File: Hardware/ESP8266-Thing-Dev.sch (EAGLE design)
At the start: 69 parts, among them J1 DNP, Q1 MMBT2222A, Q2 MMBT2222A, U1 AP2112K-3.3V, U2 ESP8266, U3 AT25SF041-SOIC8, U4 FTS31XS-U, Y1 26MHz

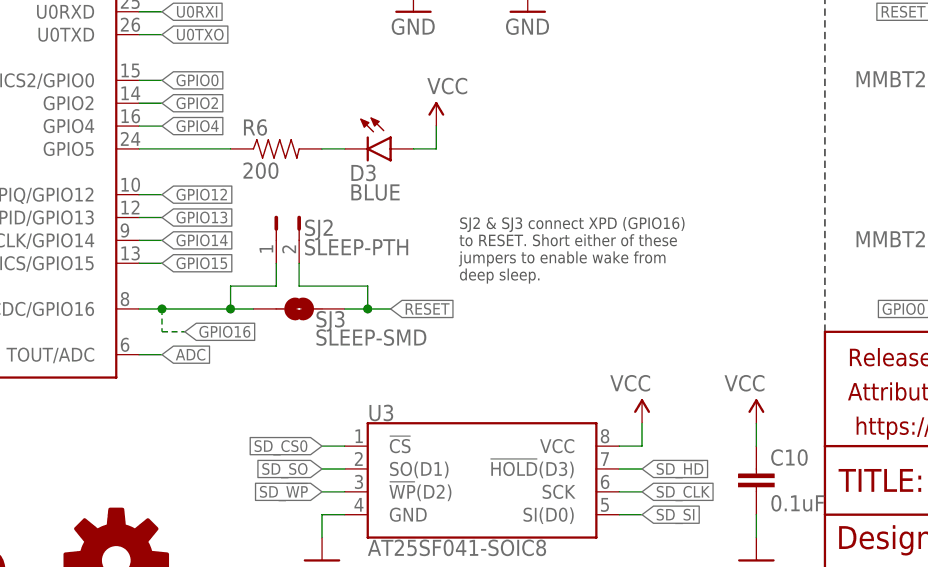
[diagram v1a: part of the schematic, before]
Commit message: Removing SJ3 - SMD sleep jumper
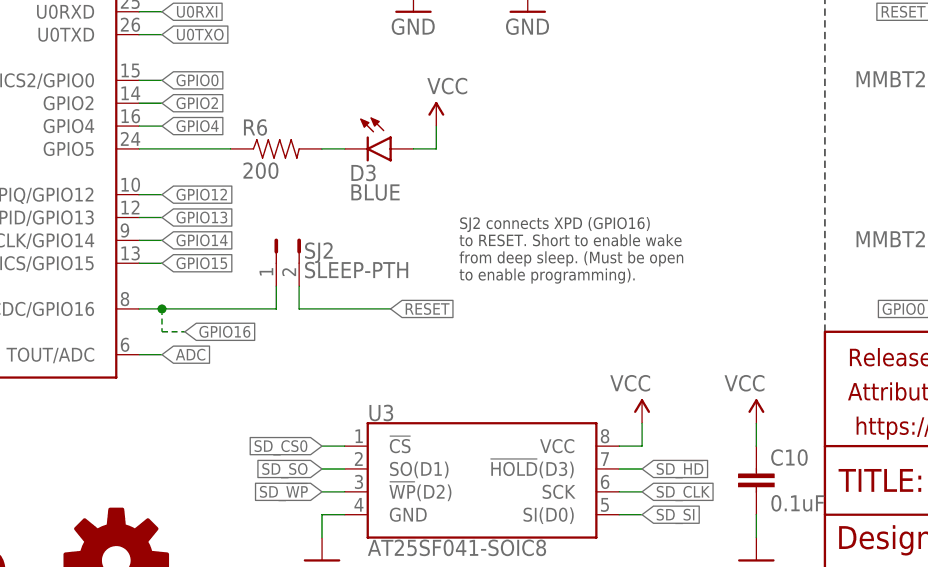
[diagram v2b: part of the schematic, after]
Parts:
- removed SJ3: SLEEP-SMD, SparkFun-Passives:JUMPER-PAD-2-NO
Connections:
- net GPIO16: no longer SJ3.1
- net RESET: no longer SJ3.2
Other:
- note added: "SJ2 connects XPD (GPIO16) to RESET. Short to enable wake from deep sleep. (Must be open to enable programming)."
- note removed: "SJ2 & SJ3 connect XPD (GPIO16) to RESET. Short either of these jumpers to enable wake from deep sleep."
- moved on the sheet: SJ2

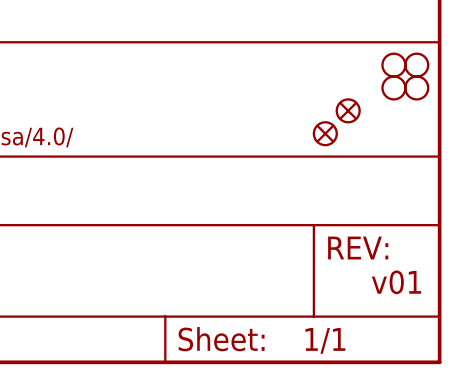
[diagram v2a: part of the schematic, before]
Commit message: Adjusting label header silk a bit
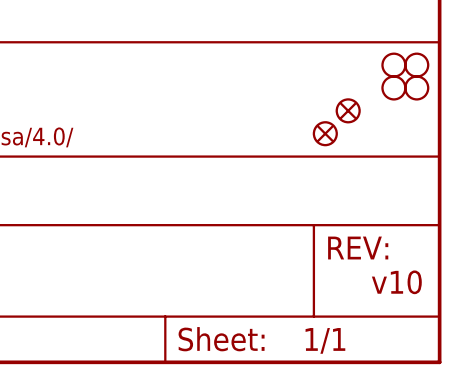
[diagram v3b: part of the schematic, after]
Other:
- note added: "v10"
- note removed: "v01"
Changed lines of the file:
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@@
 <grid distance="0.1" unitdist="inch" unit="inch" style="lines" multiple="1" display="no" altdistance="0.01" altunitdist="inch" altunit="inch"/>
 <layers>
-<layer number="1" name="Top" color="4" fill="1" visible="yes" active="no"/>
-<layer number="2" name="Route2" color="1" fill="3" visible="yes" active="no"/>
-<layer number="3" name="Route3" color="4" fill="3" visible="yes" active="no"/>
-<layer number="4" name="Route4" color="1" fill="4" visible="yes" active="no"/>
-<layer number="5" name="Route5" color="4" fill="4" visible="yes" active="no"/>
-<layer number="6" name="Route6" color="1" fill="8" visible="yes" active="no"/>
-<layer number="7" name="Route7" color="4" fill="8" visible="yes" active="no"/>
-<layer number="8" name="Route8" color="1" fill="2" visible="yes" active="no"/>
-<layer number="9" name="Route9" color="4" fill="2" visible="yes" active="no"/>
-<layer number="10" name="Route10" color="1" fill="7" visible="yes" active="no"/>
-<layer number="11" name="Route11" color="4" fill="7" visible="yes" active="no"/>
-<layer number="12" name="Route12" color="1" fill="5" visible="yes" active="no"/>
-<layer number="13" name="Route13" color="4" fill="5" visible="yes" active="no"/>
-<layer number="14" name="Route14" color="1" fill="6" visible="yes" active="no"/>
-<layer number="15" name="Route15" color="4" fill="6" visible="yes" active="no"/>
-<layer number="16" name="Bottom" color="1" fill="1" visible="yes" active="no"/>
-<layer number="17" name="Pads" color="2" fill="1" visible="yes" active="no"/>
-<layer number="18" name="Vias" color="2" fill="1" visible="yes" active="no"/>
-<layer number="19" name="Unrouted" color="6" fill="1" visible="yes" active="no"/>
-<layer number="20" name="Dimension" color="15" fill="1" visible="yes" active="no"/>
-<layer number="21" name="tPlace" color="16" fill="1" visible="yes" active="no"/>
-<layer number="22" name="bPlace" color="14" fill="1" visible="yes" active="no"/>
-<layer number="23" name="tOrigins" color="15" fill="1" visible="yes" active="no"/>
-<layer number="24" name="bOrigins" color="15" fill="1" visible="yes" active="no"/>
-<layer number="25" name="tNames" color="7" fill="1" visible="yes" active="no"/>
-<layer number="26" name="bNames" color="7" fill="1" visible="yes" active="no"/>
-<layer number="27" name="tValues" color="7" fill="1" visible="yes" active="no"/>
-<layer number="28" name="bValues" color="7" fill="1" visible="yes" active="no"/>
+<layer number="1" name="Top" color="4" fill="1" visible="no" active="no"/>
+<layer number="2" name="Route2" color="1" fill="3" visible="no" active="no"/>
+<layer number="3" name="Route3" color="4" fill="3" visible="no" active="no"/>
+<layer number="4" name="Route4" color="1" fill="4" visible="no" active="no"/>
+<layer number="5" name="Route5" color="4" fill="4" visible="no" active="no"/>
+<layer number="6" name="Route6" color="1" fill="8" visible="no" active="no"/>
+<layer number="7" name="Route7" color="4" fill="8" visible="no" active="no"/>
+<layer number="8" name="Route8" color="1" fill="2" visible="no" active="no"/>
+<layer number="9" name="Route9" color="4" fill="2" visible="no" active="no"/>
+<layer number="10" name="Route10" color="1" fill="7" visible="no" active="no"/>
+<layer number="11" name="Route11" color="4" fill="7" visible="no" active="no"/>
+<layer number="12" name="Route12" color="1" fill="5" visible="no" active="no"/>
+<layer number="13" name="Route13" color="4" fill="5" visible="no" active="no"/>
+<layer number="14" name="Route14" color="1" fill="6" visible="no" active="no"/>
+<layer number="15" name="Route15" color="4" fill="6" visible="no" active="no"/>
+<layer number="16" name="Bottom" color="1" fill="1" visible="no" active="no"/>
+<layer number="17" name="Pads" color="2" fill="1" visible="no" active="no"/>
+<layer number="18" name="Vias" color="2" fill="1" visible="no" active="no"/>
+<layer number="19" name="Unrouted" color="6" fill="1" visible="no" active="no"/>
+<layer number="20" name="Dimension" color="15" fill="1" visible="no" active="no"/>
+<layer number="21" name="tPlace" color="16" fill="1" visible="no" active="no"/>
+<layer number="22" name="bPlace" color="14" fill="1" visible="no" active="no"/>
+<layer number="23" name="tOrigins" color="15" fill="1" visible="no" active="no"/>
+<layer number="24" name="bOrigins" color="15" fill="1" visible="no" active="no"/>
+<layer number="25" name="tNames" color="7" fill="1" visible="no" active="no"/>
+<layer number="26" name="bNames" color="7" fill="1" visible="no" active="no"/>
+<layer number="27" name="tValues" color="7" fill="1" visible="no" active="no"/>
+<layer number="28" name="bValues" color="7" fill="1" visible="no" active="no"/>
 <layer number="29" name="tStop" color="7" fill="3" visible="no" active="no"/>
 <layer number="30" name="bStop" color="7" fill="6" visible="no" active="no"/>
@@
 <layer number="35" name="tGlue" color="7" fill="4" visible="no" active="no"/>
 <layer number="36" name="bGlue" color="7" fill="5" visible="no" active="no"/>
-<layer number="37" name="tTest" color="7" fill="1" visible="yes" active="no"/>
-<layer number="38" name="bTest" color="7" fill="1" visible="yes" active="no"/>
+<layer number="37" name="tTest" color="7" fill="1" visible="no" active="no"/>
+<layer number="38" name="bTest" color="7" fill="1" visible="no" active="no"/>
 <layer number="39" name="tKeepout" color="4" fill="11" visible="no" active="no"/>
 <layer number="40" name="bKeepout" color="1" fill="11" visible="no" active="no"/>
@@
 <layer number="44" name="Drills" color="7" fill="1" visible="no" active="no"/>
 <layer number="45" name="Holes" color="7" fill="1" visible="no" active="no"/>
-<layer number="46" name="Milling" color="3" fill="1" visible="yes" active="no"/>
-<layer number="47" name="Measures" color="7" fill="1" visible="yes" active="no"/>
-<layer number="48" name="Document" color="7" fill="1" visible="yes" active="no"/>
-<layer number="49" name="Reference" color="7" fill="1" visible="yes" active="no"/>
-<layer number="50" name="dxf" color="7" fill="1" visible="yes" active="no"/>
-<layer number="51" name="tDocu" color="6" fill="1" visible="yes" active="no"/>
-<layer number="52" name="bDocu" color="7" fill="1" visible="yes" active="no"/>
-<layer number="53" name="tGND_GNDA" color="7" fill="9" visible="yes" active="no"/>
-<layer number="54" name="bGND_GNDA" color="1" fill="9" visible="yes" active="no"/>
-<layer number="56" name="wert" color="7" fill="1" visible="yes" active="no"/>
-<layer number="57" name="tCAD" color="7" fill="1" visible="yes" active="no"/>
-<layer number="59" name="tCarbon" color="7" fill="1" visible="yes" active="no"/>
-<layer number="60" name="bCarbon" color="7" fill="1" visible="yes" active="no"/>
+<layer number="46" name="Milling" color="3" fill="1" visible="no" active="no"/>
+<layer number="47" name="Measures" color="7" fill="1" visible="no" active="no"/>
+<layer number="48" name="Document" color="7" fill="1" visible="no" active="no"/>
+<layer number="49" name="Reference" color="7" fill="1" visible="no" active="no"/>
+<layer number="50" name="dxf" color="7" fill="1" visible="no" active="no"/>
+<layer number="51" name="tDocu" color="6" fill="1" visible="no" active="no"/>
+<layer number="52" name="bDocu" color="7" fill="1" visible="no" active="no"/>
+<layer number="53" name="tGND_GNDA" color="7" fill="9" visible="no" active="no"/>
+<layer number="54" name="bGND_GNDA" color="1" fill="9" visible="no" active="no"/>
+<layer number="56" name="wert" color="7" fill="1" visible="no" active="no"/>
+<layer number="57" name="tCAD" color="7" fill="1" visible="no" active="no"/>
+<layer number="59" name="tCarbon" color="7" fill="1" visible="no" active="no"/>
+<layer number="60" name="bCarbon" color="7" fill="1" visible="no" active="no"/>
 <layer number="90" name="Modules" color="5" fill="1" visible="yes" active="yes"/>
 <layer number="91" name="Nets" color="2" fill="1" visible="yes" active="yes"/>
@@
 lots of power.)</text>
 <text x="172.72" y="10.16" size="2.54" layer="94" align="top-left">Jim Lindblom</text>
-<text x="241.3" y="10.16" size="2.54" layer="94" align="top-left">v01</text>
+<text x="241.3" y="10.16" size="2.54" layer="94" align="top-left">v10</text>
 <text x="139.7" y="95.504" size="1.778" layer="97">DNP</text>
 </plain>

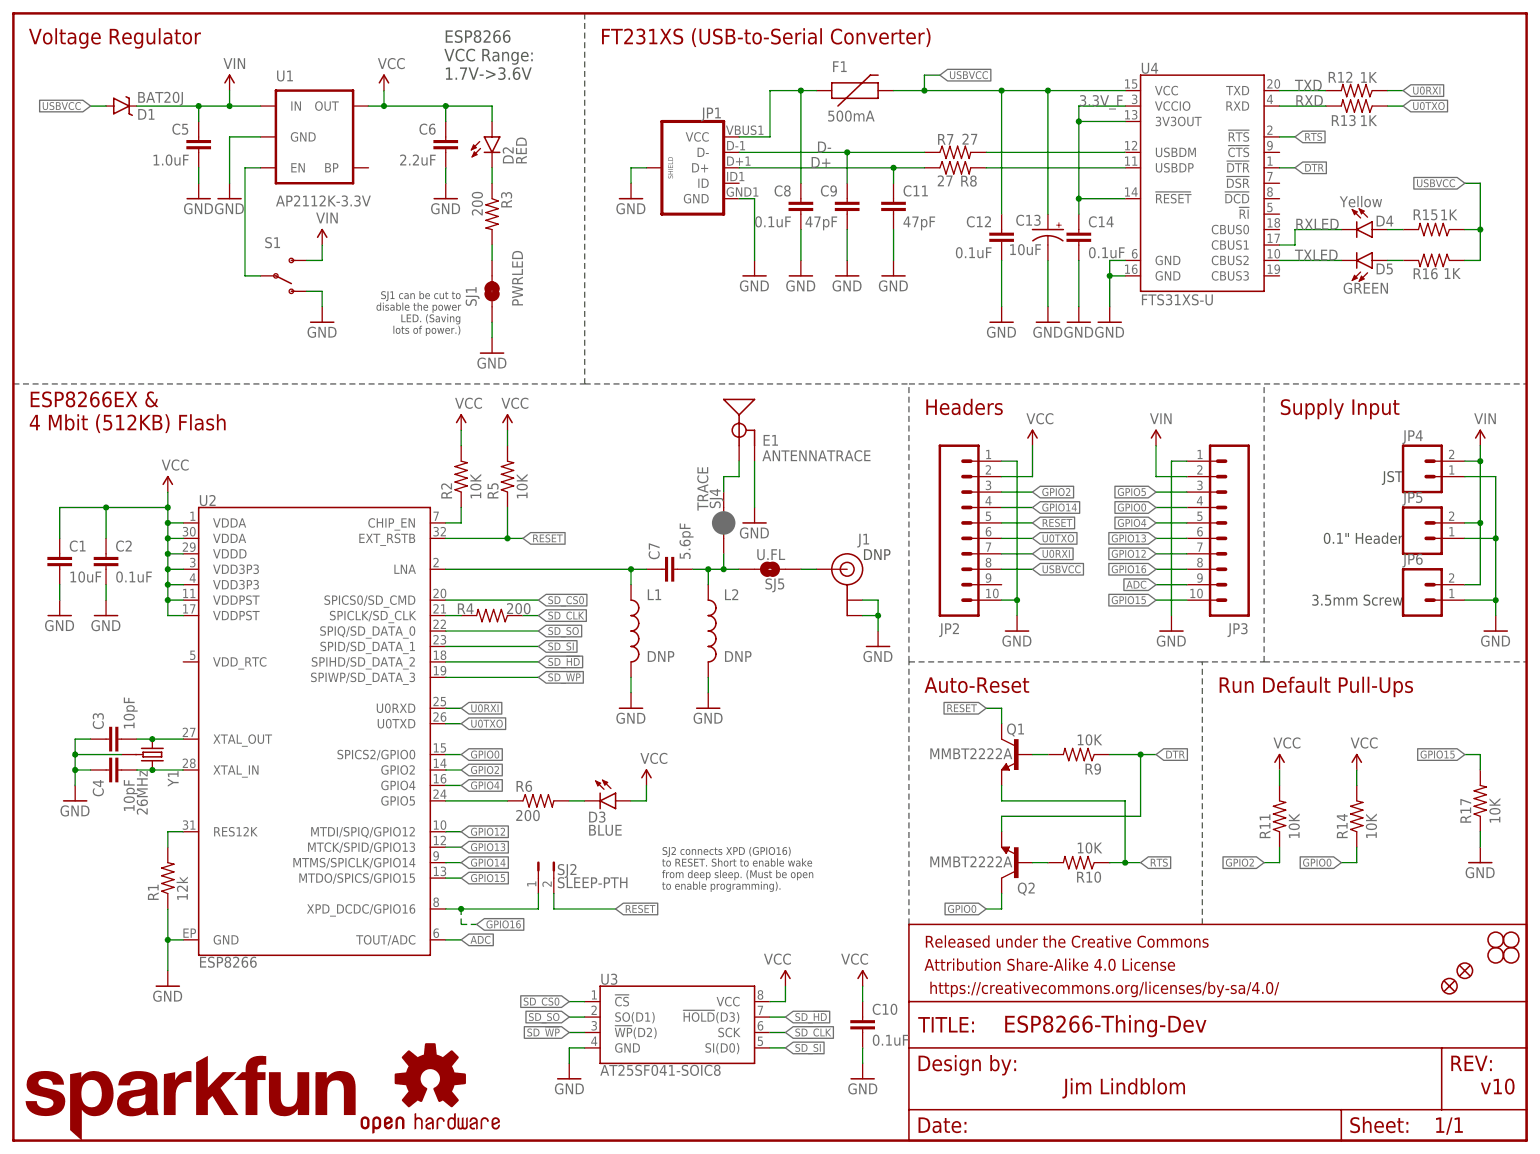
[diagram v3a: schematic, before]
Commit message: Schematic cleanup, tweaking silkscreen
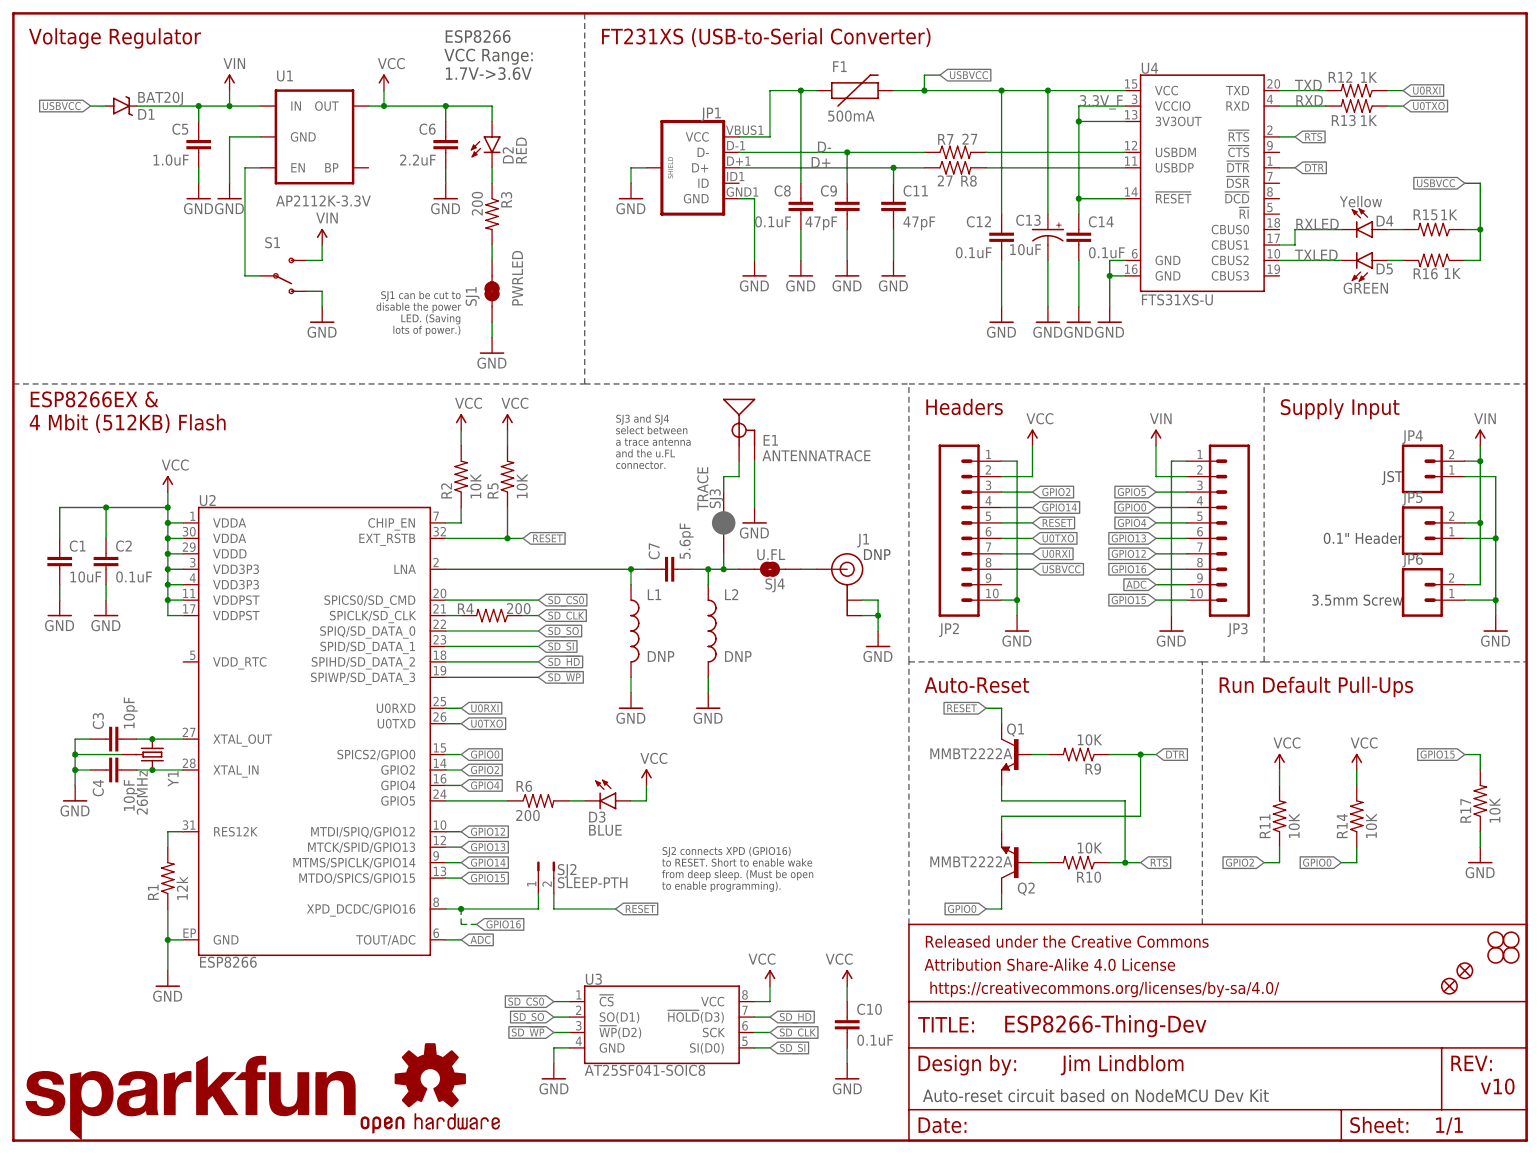
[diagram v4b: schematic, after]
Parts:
- removed SJ5: U.FL, SparkFun-Passives:JUMPER-PAD-2-NO
- added SJ3: TRACE, SparkFun-Passives:JUMPER-PAD-2-NC_BY_PASTENO-SILK
- JP5: device SparkFun-Connectors:M02PTH -> SparkFun-Connectors:M021X02_NO_SILK
- SJ4: value TRACE -> U.FL; device SparkFun-Passives:JUMPER-PAD-2-NC_BY_PASTENO-SILK -> SparkFun-Passives:JUMPER-PAD-2-NO
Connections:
- net ANT: now also SJ4.1; no longer SJ5.1
- net LNA2: now also SJ3.1, SJ4.2; no longer SJ4.1, SJ5.2
- net TRACE_ANT: now also SJ3.2; no longer SJ4.2
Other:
- note added: "Auto-reset circuit based on NodeMCU Dev Kit"
- note added: "SJ3 and SJ4 select between a trace antenna and the u.FL connector."
- moved on the sheet: C10, U3
